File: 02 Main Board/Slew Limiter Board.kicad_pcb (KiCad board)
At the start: 2 copper layers, 18 x 116 mm, 21 parts, among them J1 Input, J2 Output, SW1 ON-OFF-ON, U1 TL072

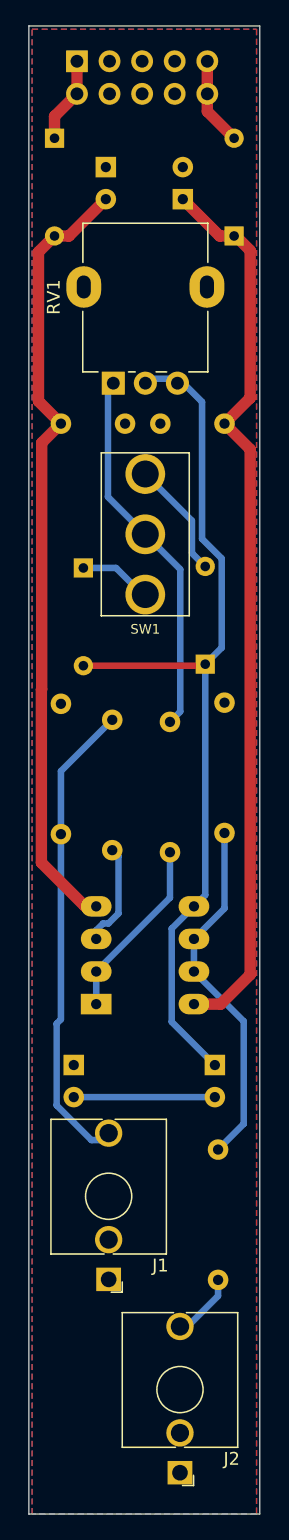
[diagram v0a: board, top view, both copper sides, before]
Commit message: misc changes see description
Slightly shrink board (no moving of components)
Increase silkscreen text size
Increase edge cuts line thickness
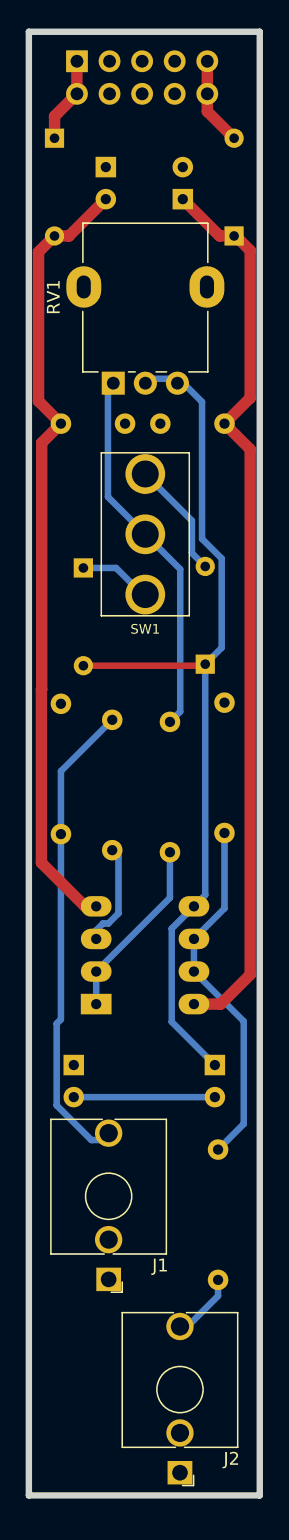
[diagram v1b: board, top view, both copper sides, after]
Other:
- board size 18 x 116 mm -> 18 x 114.1 mm

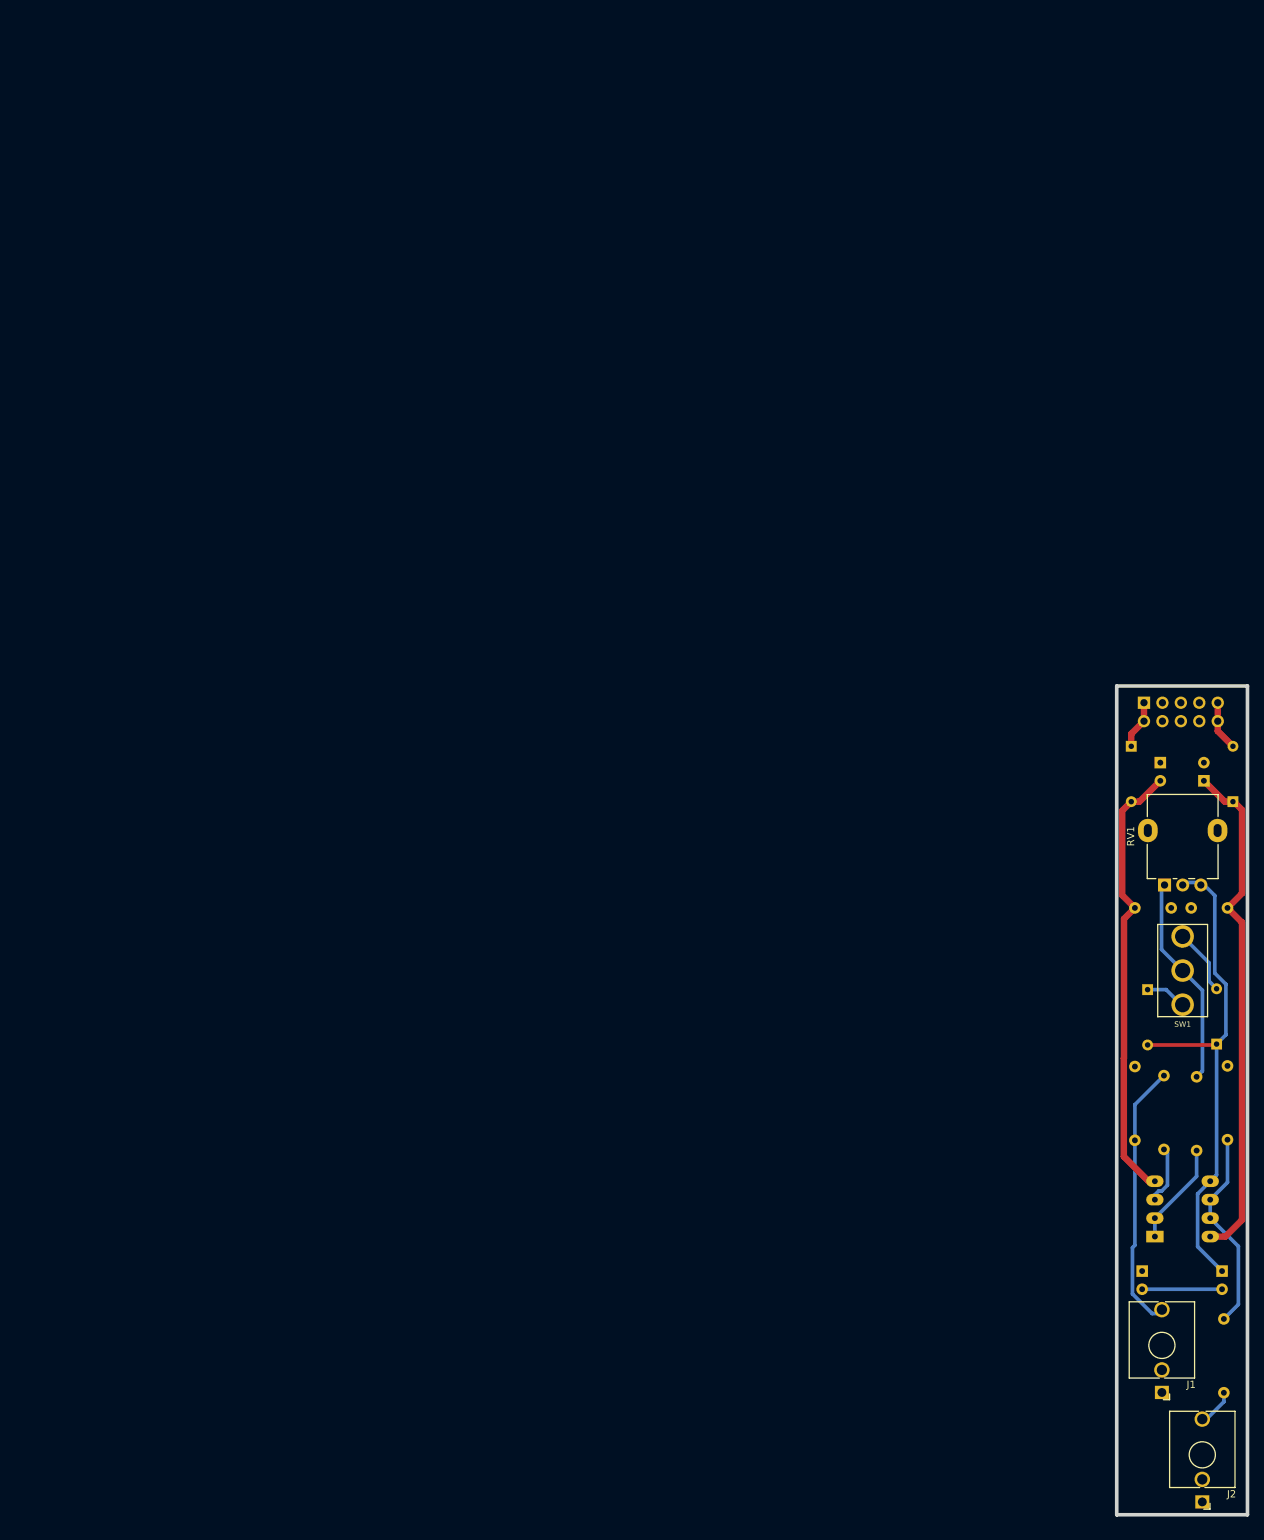
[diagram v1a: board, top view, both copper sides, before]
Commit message: Update to v1.2
Many changes, see readme for list
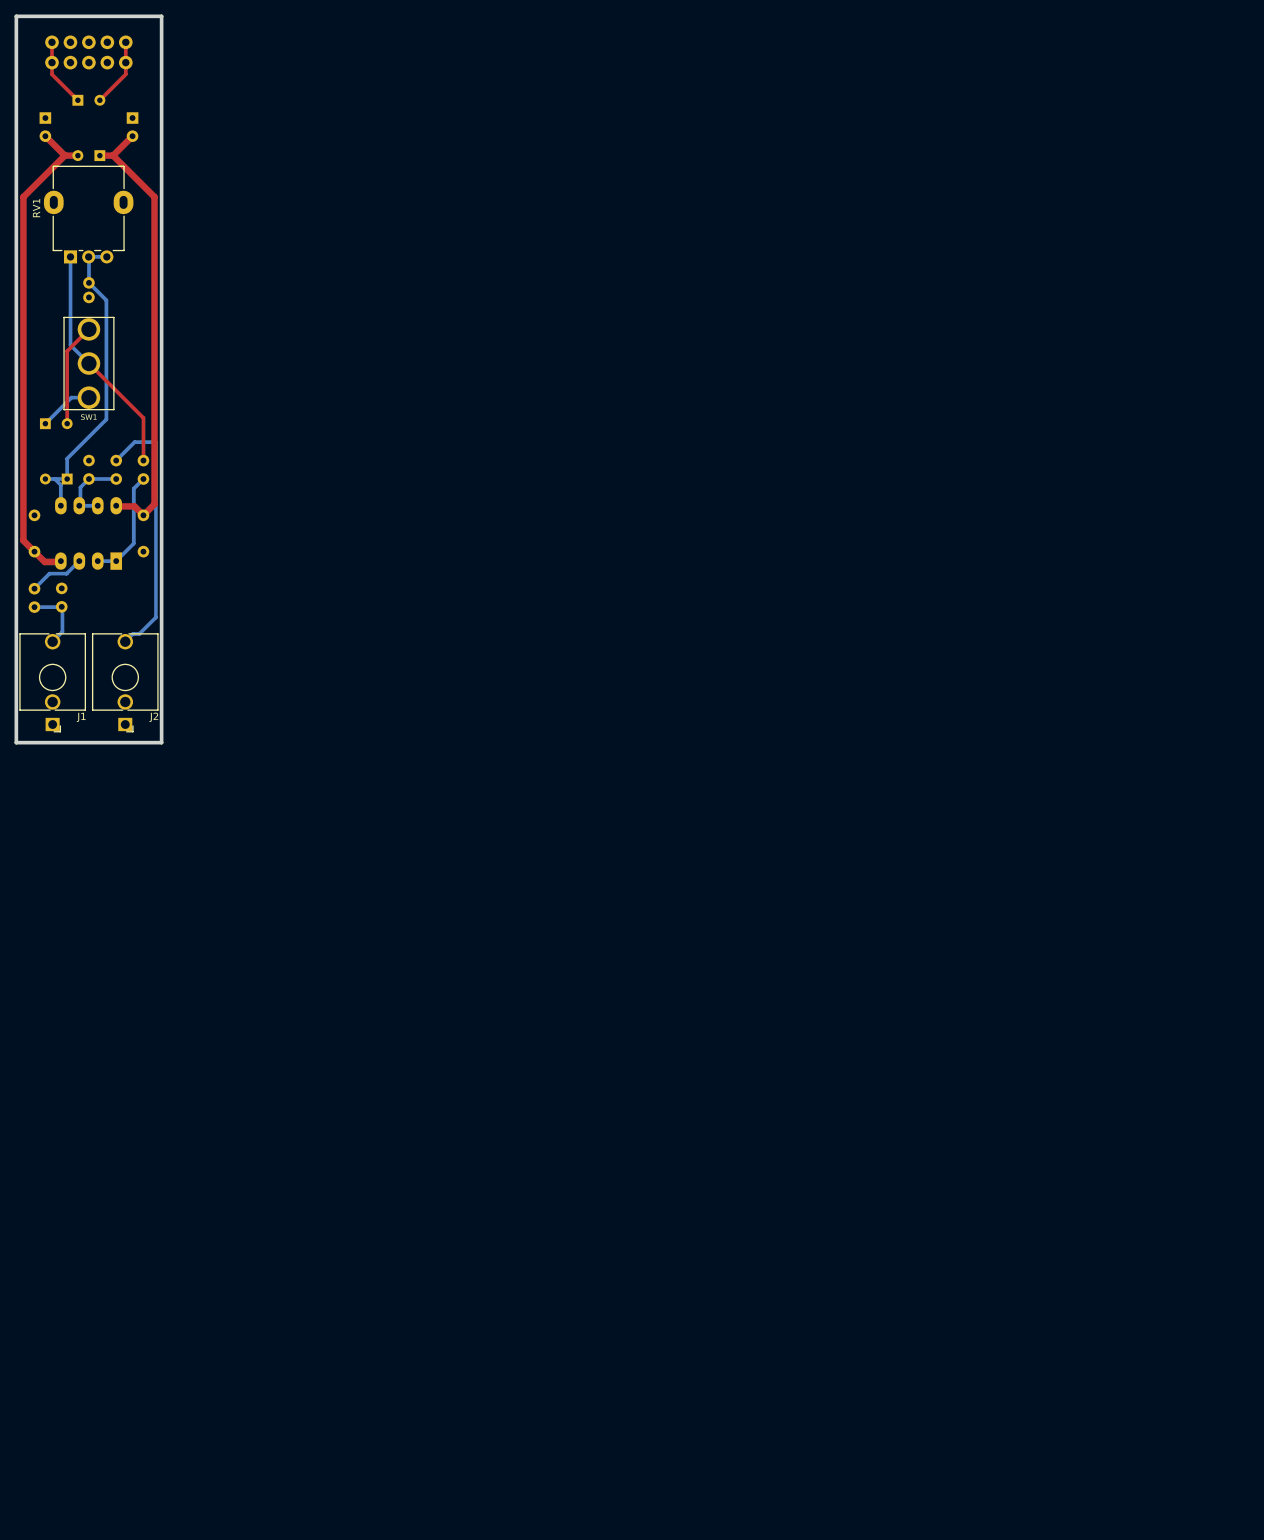
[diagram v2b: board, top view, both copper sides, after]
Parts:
- removed the C4 at (144.0, 72.8)
- removed C6: 10uf, Capacitor_THT:CP_Radial_D5.0mm_P2.50mm
- removed the R5 at (156.2, 139.5)
- added C3: 4.7uf, Capacitor_THT:C_Radial_D5.0mm_H11.0mm_P2.00mm, B.Cu at (0.00, -13.3)
- added R2: 100r, Resistor_THT:R_Axial_DIN0207_L6.3mm_D2.5mm_P2.54mm_Vertical, B.Cu at (3.75, 13.7)
- C5: value 10uf -> 100nf; footprint Capacitor_THT:CP_Radial_D5.0mm_P2.50mm -> Capacitor_THT:C_Disc_D5.0mm_W2.5mm_P5.00mm
- JP1: footprint Connector_PinHeader_2.54mm:PinHeader_2x05_P2.54mm_Vertical -> mainboard:Eurorack_Power
- R1: renamed from R2; footprint Resistor_THT:R_Axial_DIN0207_L6.3mm_D2.5mm_P10.16mm_Horizontal -> Resistor_THT:R_Axial_DIN0207_L6.3mm_D2.5mm_P2.54mm_Vertical
- R3: renamed from R1; footprint Resistor_THT:R_Axial_DIN0207_L6.3mm_D2.5mm_P10.16mm_Horizontal -> Resistor_THT:R_Axial_DIN0207_L6.3mm_D2.5mm_P2.54mm_Vertical
- R4: footprint Resistor_THT:R_Axial_DIN0207_L6.3mm_D2.5mm_P10.16mm_Horizontal -> Resistor_THT:R_Axial_DIN0207_L6.3mm_D2.5mm_P2.54mm_Vertical
- R5: renamed from R3; footprint Resistor_THT:R_Axial_DIN0207_L6.3mm_D2.5mm_P10.16mm_Horizontal -> Resistor_THT:R_Axial_DIN0207_L6.3mm_D2.5mm_P2.54mm_Vertical
- moved C5 191.2 mm to (-7.50, 23.7), turned to 90 degrees
- moved J2 186.8 mm to (5.00, 41.0)
- moved R3 181.2 mm to (0.00, 13.7)
- moved D1 179.6 mm to (1.50, -30.8)
- moved J1 178.3 mm to (-5.00, 41.0)
- moved C2 177.3 mm to (-6.00, -36.0)
- moved D3 176.3 mm to (-3.00, 13.7)
- moved RV1 173.7 mm to (0.00, -24.5)
- moved R5 173.6 mm to (-7.50, 28.8), turned to 270 degrees
- moved C1 173.4 mm to (6.00, -36.0), turned to 270 degrees
- moved SW1 172.2 mm to (0.00, -2.20)
- moved JP1 170.6 mm to (-0.01, -45.0), turned to 0 degrees
- moved D4 170.6 mm to (-6.00, 6.08)
- moved U1 170.6 mm to (3.75, 25.0), turned to 90 degrees
- moved D2 170.1 mm to (-1.52, -38.4)
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- renumbered C3 to C4
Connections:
- C1 pad 1: +12V -> GND
- C1 pad 2: GND -> +12V
- C4 pad 1: GND -> +12V
- C4 pad 2: +12V -> GND
- C5 pad 1: Net-(C5-Pad1) -> -12V
- C5 pad 2: Net-(C5-Pad2) -> GND
- D3 pad 1: Net-(C5-Pad1) -> Net-(C3-Pad1)
- D4 pad 2: Net-(C5-Pad1) -> Net-(C3-Pad1)
- R1 pad 1: Net-(R2-Pad1) (its old number) -> Net-(R1-Pad1)
- R1 pad 2: Net-(R2-Pad2) -> Net-(R1-Pad2)
- R4 pad 1: Net-(J1-PadT) -> GND
- R4 pad 2: GND -> Net-(J1-PadT)
- RV1 pad 1: Net-(R2-Pad1) (its old number) -> Net-(R1-Pad2)
- RV1 pad 2: Net-(C5-Pad1) -> Net-(C3-Pad1)
- RV1 pad 3: Net-(C5-Pad1) -> Net-(C3-Pad1)
- SW1 pad 2: Net-(R2-Pad1) (its old number) -> Net-(R1-Pad2)
- U1 pad 1: Net-(R2-Pad2) -> Net-(R1-Pad1)
- U1 pad 2: Net-(R2-Pad2) -> Net-(R1-Pad1)
- U1 pad 5: Net-(C5-Pad1) -> Net-(C3-Pad1)
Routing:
- net Net-(C5-Pad1): track 69.9 -> 0.00 mm
- net Net-(C3-Pad1): track 0.00 -> 43.4 mm
- net Net-(R1-Pad2): track 0.00 -> 32.2 mm
- net Net-(J2-PadT): track 5.49 -> 36.3 mm
- net Net-(R2-Pad1) (its old number): track 29.6 -> 0.00 mm
- net Net-(J1-PadT): track 37.1 -> 9.17 mm
- net Net-(R2-Pad1): track 28.1 -> 10.6 mm
- net Net-(R1-Pad1): track 0.00 -> 15.4 mm
- net Net-(R2-Pad2): track 14.2 -> 0.00 mm
- net Net-(C5-Pad2): track 11.0 -> 0.00 mm
- net +12V: track 70.5 -> 62.4 mm
- net -12V: track 61.6 -> 67.4 mm
- net Net-(D3-Pad2): track 10.3 -> 14.2 mm
- net Net-(D2-Pad1): track 6.72 -> 9.46 mm
- net Net-(D1-Pad2): track 6.87 -> 9.46 mm
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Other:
- board size 18 x 114.1 mm -> 20 x 100 mm
- board text added: "JLCJLCJLCJLC"
- board text added: "Slew Limiter v1.2 Bell Lab"
- board text removed: "-12v"
- board text removed: "Slew Limiter v1.0 Bell Lab"
